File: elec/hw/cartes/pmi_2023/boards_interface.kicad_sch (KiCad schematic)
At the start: 39 parts, among them J10 Conn_01x01_Pin, J11 Conn_01x01_Socket, J12 Conn_01x01_Pin, J13 Conn_01x01_Pin, J14 Conn_01x01_Socket, J15 Conn_01x01_Socket, J16 Conn_01x01_Pin, J17 Conn_01x01_Pin, J18 Conn_01x01_Pin, J19 Conn_01x01_Pin, J20 Conn_01x01_Socket, J21 Conn_01x01_Socket, J22 Conn_01x01_Socket, J23 Conn_01x01_Pin, J24 Conn_01x01_Pin, J25 Conn_01x01_Pin, J26 Conn_01x01_Pin, J27 Conn_01x01_Socket, J28 Conn_01x01_Socket, J29 Conn_01x01_Socket, J30 Conn_01x01_Socket, J31 Conn_01x01_Pin, J32 Conn_01x01_Pin, J33 Conn_01x01_Socket, J34 Conn_01x01_Socket, J35 Conn_01x01_Pin, J36 Conn_01x01_Socket, J37 Conn_01x01_Pin, J38 Conn_01x01_Socket, J39 Conn_01x01_Pin, J40 Conn_01x01_Pin, J41 Conn_01x01_Socket, J42 Conn_01x01_Socket, J43 Conn_01x01_Socket, J44 Conn_01x01_Pin, J45 Conn_01x01_Socket, J46 Conn_01x01_Pin, J9 Conn_01x01_Socket

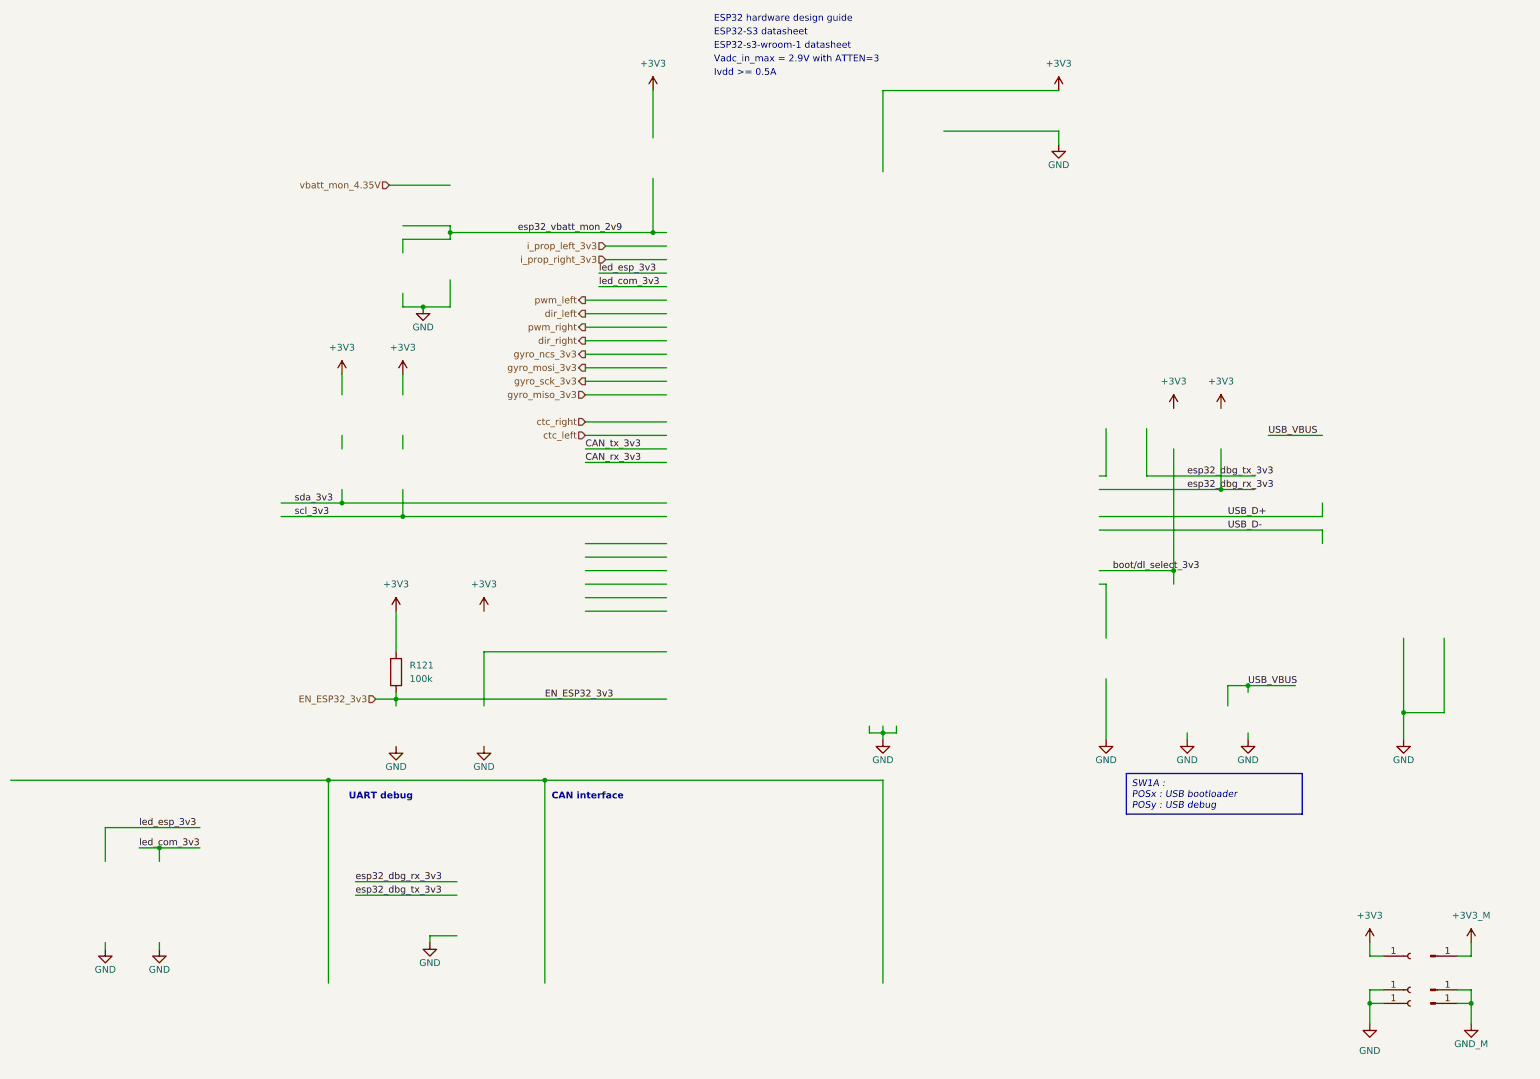
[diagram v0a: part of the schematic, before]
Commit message: pmi layout (WIP)
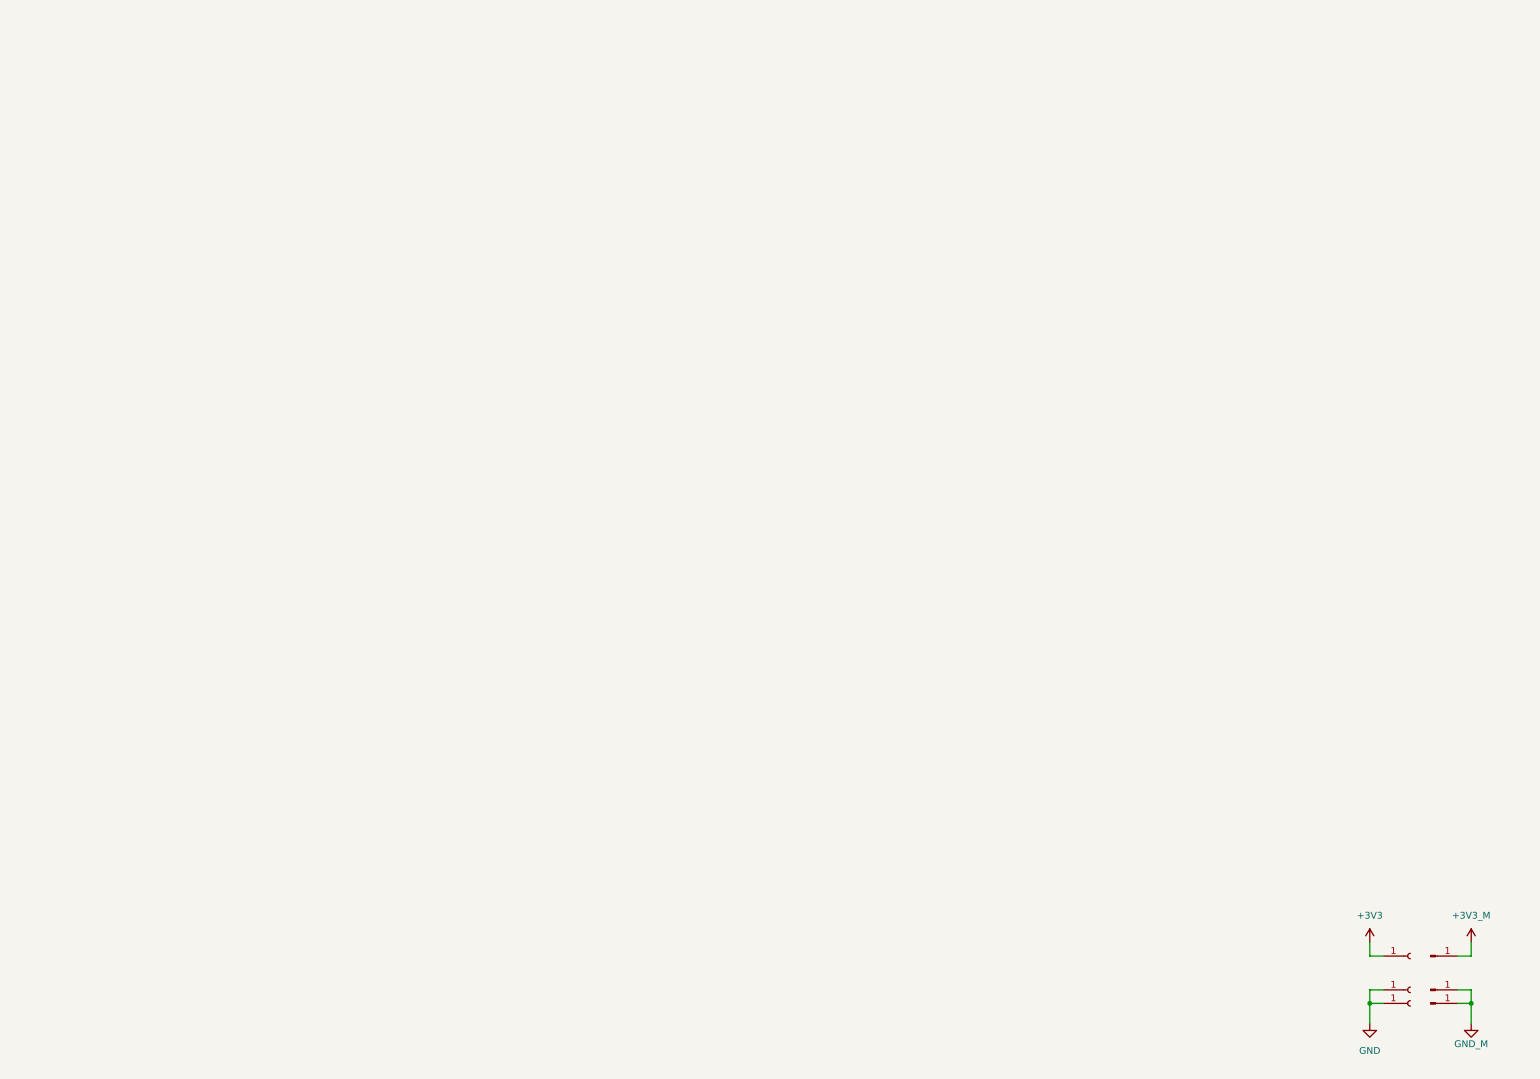
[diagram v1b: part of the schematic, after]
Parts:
- removed R121: 100k, cocotter_resistor:r0603_reflow, symbol cocotter_resistors:R_100k_0603_1%
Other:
- note removed: "CAN interface"
- note removed: "ESP32 hardware design guide"
- note removed: "ESP32-S3 datasheet"
- note removed: "ESP32-s3-wroom-1 datasheet"
- note removed: "Ivdd >= 0.5A"
- note removed: "UART debug"
- note removed: "Vadc_in_max = 2.9V with ATTEN=3"

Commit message: wip
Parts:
- added J47: Conn_01x01_Pin, cocotter_others:board_to_module_small, symbol Connector:Conn_01x01_Pin
- added J48: Conn_01x01_Socket, cocotter_others:board_to_module_small, symbol Connector:Conn_01x01_Socket
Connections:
- net com/vbatt_mon_4.35V: now also J47.1 (Pin_1)
- new net vbatt_mon_4.35V: J48.1 (Pin_1)
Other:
- sheet Sensor module ports: added gyro_irq_3v3; removed none
- sheet com ports: added emergency_stop_3v3, gyro_irq_3v3, start_robot_3v3; removed esp32_rx1_3v3, esp32_rx2_3v3, esp32_tx1_3v3, esp32_tx2_3v3
- sheet interface ports: added emergency_stop_3v3, start_robot_3v3; removed none

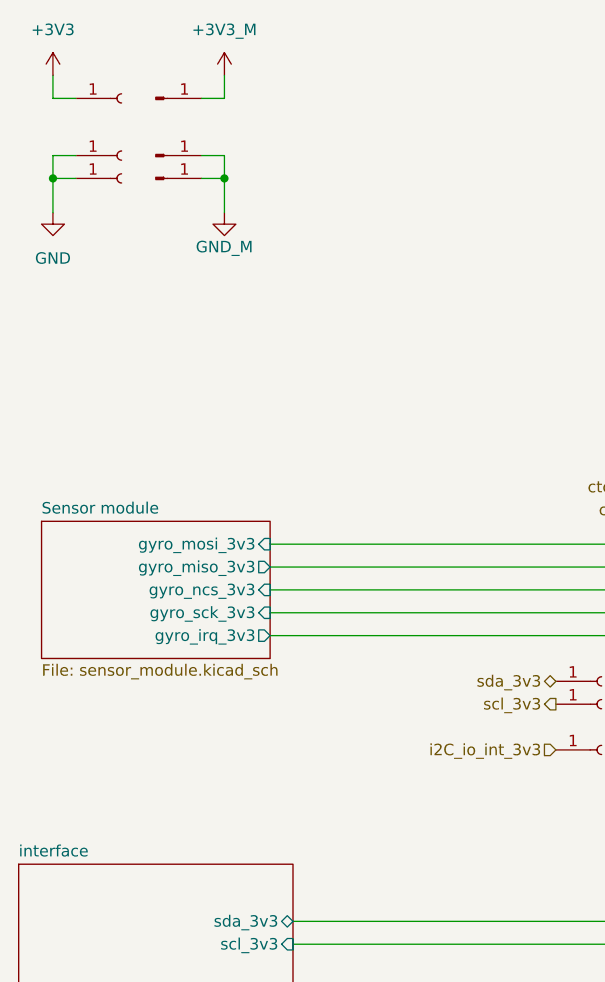
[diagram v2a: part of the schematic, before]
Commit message: front and back tof added, selector changed, ready to route
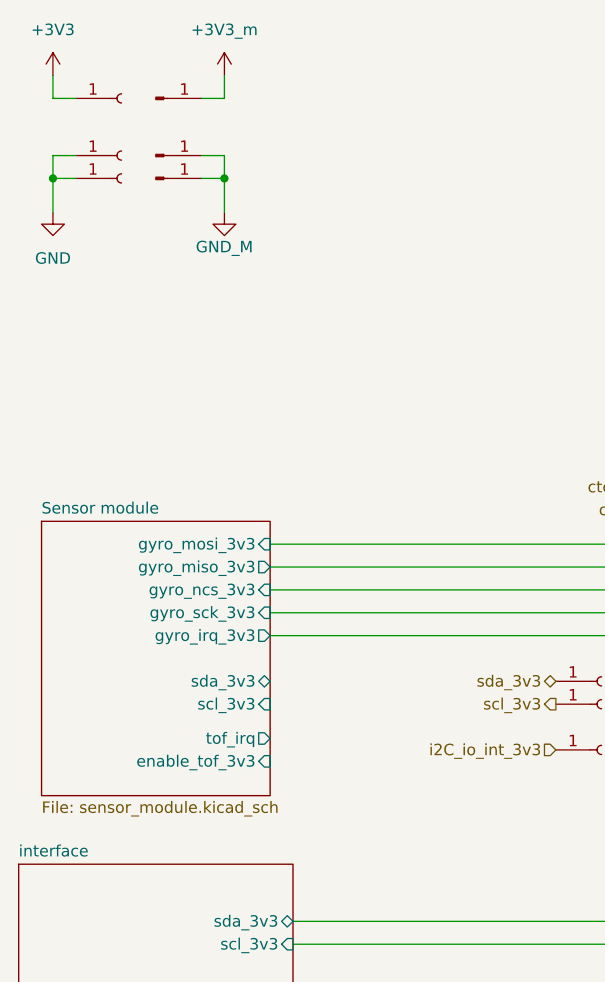
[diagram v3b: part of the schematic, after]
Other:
- sheet Sensor module ports: added enable_tof_3v3, scl_3v3, sda_3v3, tof_irq; removed none

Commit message: wip
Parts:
- removed J10, J12, J13, J16, J17, J18, J19, J23, J24, J25, J26, J31, J32, J35, J37, J39, J40, J44, J46, J47: Conn_01x01_Pin, cocotter_others:board_to_module_small, symbol Connector:Conn_01x01_Pin
- removed J11, J14, J15, J20, J21, J22, J27, J28, J29, J30, J33, J34, J36, J38, J41, J42, J43, J45, J48, J9: Conn_01x01_Socket, cocotter_others:board_to_module_small, symbol Connector:Conn_01x01_Socket
- added J49, J50: ~, pmi_2023_specific:pmi_2023_interconnection, symbol pmi_2023_specific:interconnect
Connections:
- net +3V3: now also J50.10 (P3V3)
- net +3V3_m: now also J49.10 (P3V3)
- net GND: now also J50.13 (GND), J50.7 (GND)
- net GND_M: now also J49.13 (GND), J49.7 (GND)
- net com/ctc_left: now also J49.20 (ctc_left_3v3)
- net com/ctc_right: now also J49.1 (ctc_right_3v3)
- net com/dir_left: now also J49.5 (DIR_left_3v3)
- net com/dir_right: now also J49.12 (dir_right_3v3)
- net com/i_prop_left_3v3: now also J49.6 (i_prop_left_3v3)
- net com/i_prop_right_3v3: now also J49.14 (i_prop_righ_3v3)
- net com/left_encod_A_3v3: now also J49.8 (left_encod_A_3v3)
- net com/left_encod_B_3v3: now also J49.9 (left_encod_B_3v3)
- net com/pwm_left: now also J49.4 (PWM_left_3v3)
- net com/pwm_right: now also J49.11 (pwm_right_3v3)
- net com/right_encod_A_3v3: now also J49.19 (right_encod_A_3v3)
- net com/right_encod_B_3v3: now also J49.18 (right_encod_B_3v3)
- net com/vbatt_mon_4.35V: now also J49.2 (vbat_mon_4.35V)
- net ctc_left: now also J50.20 (ctc_left_3v3)
- net ctc_right: now also J50.1 (ctc_right_3v3)
- net dir_left: now also J50.5 (DIR_left_3v3)
- net dir_right: now also J50.12 (dir_right_3v3)
- net i2C_io_int_3v3: now also J50.17 (i2c_to_int_3v3)
- net i_prop_left_3v3: now also J50.6 (i_prop_left_3v3)
- net i_prop_right_3v3: now also J50.14 (i_prop_righ_3v3)
- net left_encod_A_3v3: now also J50.8 (left_encod_A_3v3)
- net left_encod_B_3v3: now also J50.9 (left_encod_B_3v3)
- net pwm_left: now also J50.4 (PWM_left_3v3)
- net pwm_right: now also J50.11 (pwm_right_3v3)
- net right_encod_A_3v3: now also J50.19 (right_encod_A_3v3)
- net right_encod_B_3v3: now also J50.18 (right_encod_B_3v3)
- net scl_3v3: now also J50.15 (scl_3v3)
- net sda_3v3: now also J50.16 (sda_3v3)
- net tof_irq: now also J50.3 (tof_irq_3v3)
- net vbatt_mon_4.35V: now also J50.2 (vbat_mon_4.35V)
- new net i2c_io_int_3v3: J49.17 (i2c_to_int_3v3)
- new net scl_top_3v3: J49.15 (scl_3v3)
- new net sda_top_3v3: J49.16 (sda_3v3)
- new net tof_irq_3v3: J49.3 (tof_irq_3v3)
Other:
- sheet com ports: added conf3_3v3, enable_tof_3v3; removed none
- sheet interface ports: added conf3; removed none

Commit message: added oled display power supply res selectors, jlcpcb refs : wip
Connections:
- net +3V3_m is gone; now on net +3V3: J49.10 (P3V3)
- net GND_M is gone; now on net GND: J49.13 (GND), J49.7 (GND)
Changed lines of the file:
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@@
 			)
 		)
-		(property "Value" "GND_M"
+		(property "Value" "GND"
 			(at 186.69 118.11 0)
 			(effects
@@
 		(dnp no)
 		(property "Reference" "J49"
-			(at 209.55 61.214 0)
+			(at 210.058 52.324 0)
 			(effects
 				(font
@@
 		(dnp no)
 		(property "Reference" "J50"
-			(at 225.806 60.706 0)
+			(at 225.806 52.324 0)
 			(effects
 				(font
@@
 			)
 		)
-		(property "Value" "+3V3_m"
+		(property "Value" "+3V3"
 			(at 173.99 52.07 0)
 			(effects

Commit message: reset button added to esp32 reset. uart prog connector replaces ftdi one
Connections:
- net +3V3: no longer J49.10 (P3V3)
- net GND: no longer J49.13 (GND), J49.7 (GND)
- new net +3V3_m: J49.10 (P3V3)
- new net GND_m: J49.13 (GND), J49.7 (GND)
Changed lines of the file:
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@@
-	)
-	(symbol
-		(lib_id "power:GND")
-		(at 186.69 114.3 0)
-		(unit 1)
-		(exclude_from_sim no)
-		(in_bom yes)
-		(on_board yes)
-		(dnp no)
-		(property "Reference" "#PWR099"
-			(at 186.69 120.65 0)
-			(effects
-				(font
-					(size 1.27 1.27)
-				)
-				(hide yes)
-			)
-		)
-		(property "Value" "GND"
-			(at 186.69 118.11 0)
-			(effects
-				(font
-					(size 1.27 1.27)
-				)
-			)
-		)
-		(property "Footprint" ""
-			(at 186.69 114.3 0)
-			(effects
-				(font
-					(size 1.27 1.27)
-				)
-				(hide yes)
-			)
-		)
-		(property "Datasheet" ""
-			(at 186.69 114.3 0)
-			(effects
-				(font
-					(size 1.27 1.27)
-				)
-				(hide yes)
-			)
-		)
-		(property "Description" "Power symbol creates a global label with name \"GND\" , ground"
-			(at 186.69 114.3 0)
-			(effects
-				(font
-					(size 1.27 1.27)
-				)
-				(hide yes)
-			)
-		)
-		(pin "1"
-		)
-		(instances
-			(project "pmi_2023"
-				(path "/334a657f-c66c-4260-9567-14f1c99913d7/9da1923e-9bb0-4408-8ee2-582c85dcd497"
-					(reference "#PWR099")
-					(unit 1)
-				)
-			)
-		)
 	)
 	(symbol
@@
 	)
 	(symbol
+		(lib_id "pmi_2023_specific:GND_m")
+		(at 186.69 114.3 0)
+		(unit 1)
+		(exclude_from_sim no)
+		(in_bom yes)
+		(on_board yes)
+		(dnp no)
+		(fields_autoplaced yes)
+		(property "Reference" "#PWR091"
+			(at 186.69 120.65 0)
+			(effects
+				(font
+					(size 1.27 1.27)
+				)
+				(hide yes)
+			)
+		)
+		(property "Value" "GND_m"
+			(at 186.69 119.38 0)
+			(effects
+				(font
+					(size 1.27 1.27)
+				)
+			)
+		)
+		(property "Footprint" ""
+			(at 186.69 114.3 0)
+			(effects
+				(font
+					(size 1.27 1.27)
+				)
+				(hide yes)
+			)
+		)
+		(property "Datasheet" ""
+			(at 186.69 114.3 0)
+			(effects
+				(font
+					(size 1.27 1.27)
+				)
+				(hide yes)
+			)
+		)
+		(property "Description" "Power symbol creates a global label with name \"GND\" , ground"
+			(at 186.69 114.3 0)
+			(effects
+				(font
+					(size 1.27 1.27)
+				)
+				(hide yes)
+			)
+		)
+		(pin "1"
+		)
+		(instances
+			(project "pmi_2023"
+				(path "/334a657f-c66c-4260-9567-14f1c99913d7/9da1923e-9bb0-4408-8ee2-582c85dcd497"
+					(reference "#PWR091")
+					(unit 1)
+				)
+			)
+		)
+	)
+	(symbol
 		(lib_id "pmi_2023_specific:interconnect")
 		(at 198.12 85.09 0)
@@
 		(dnp no)
 		(property "Reference" "J49"
-			(at 210.058 52.324 0)
-			(effects
-				(font
-					(size 1.27 1.27)
-				)
-				(justify left)
+			(at 205.994 125.476 0)
+			(effects
+				(font
+					(size 1.27 1.27)
+				)
 			)
 		)
 		(property "Value" "~"
-			(at 214.63 85.09 0)
-			(effects
-				(font
-					(size 1.27 1.27)
-				)
-				(justify left)
+			(at 198.12 96.52 0)
+			(effects
+				(font
+					(size 1.27 1.27)
+				)
 			)
 		)
 		(property "Footprint" "pmi_2023_specific:pmi_2023_interconnection"
-			(at 198.12 96.52 0)
+			(at 198.12 93.98 0)
 			(effects
 				(font
@@
 		(dnp no)
 		(property "Reference" "J50"
-			(at 225.806 52.324 0)
-			(effects
-				(font
-					(size 1.27 1.27)
-				)
-				(justify left)
+			(at 229.616 125.476 0)
+			(effects
+				(font
+					(size 1.27 1.27)
+				)
 			)
 		)
 		(property "Value" "~"
-			(at 220.98 85.09 0)
-			(effects
-				(font
-					(size 1.27 1.27)
-				)
-				(justify left)
+			(at 237.49 96.52 0)
+			(effects
+				(font
+					(size 1.27 1.27)
+				)
 			)
 		)
 		(property "Footprint" "pmi_2023_specific:pmi_2023_interconnection"
-			(at 237.49 96.52 0)
+			(at 237.49 93.98 0)
 			(effects
 				(font
@@
 	)
 	(symbol
-		(lib_id "power:+3V3")
+		(lib_id "pmi_2023_specific:+3V3_m")
 		(at 173.99 57.15 0)
 		(unit 1)
@@
 		(dnp no)
 		(fields_autoplaced yes)
-		(property "Reference" "#PWR098"
+		(property "Reference" "#PWR097"
 			(at 173.99 60.96 0)
 			(effects
@@
 			)
 		)
-		(property "Value" "+3V3"
+		(property "Value" "+3V3_m"
 			(at 173.99 52.07 0)
 			(effects
@@
 			)
 		)
-		(property "Description" "Power symbol creates a global label with name \"+3V3\""
+		(property "Description" "Power symbol creates a global label with name \"+3V3_m\""
 			(at 173.99 57.15 0)
 			(effects
@@
 			(project "pmi_2023"
 				(path "/334a657f-c66c-4260-9567-14f1c99913d7/9da1923e-9bb0-4408-8ee2-582c85dcd497"
-					(reference "#PWR098")
-					(unit 1)
-				)
+					(reference "#PWR097")
+					(unit 1)
+				)

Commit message: pmi2023 : drc cleanup
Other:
- sheet Sensor module ports: added enable_back_tof_3v3, enable_front_tof_3v3; removed enable_tof_3v3
- sheet com ports: added enable_back_tof_3v3, enable_front_tof_3v3; removed enable_tof_3v3
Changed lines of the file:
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@@
+	(wire
+		(pts
+			(xy 57.15 100.33) (xy 113.03 100.33)
+		)
+		(stroke
+			(width 0)
+			(type default)
+		)
+	)
 	(wire
 		(pts
@@
 			)
 		)
-		(pin "enable_tof_3v3" input
+		(pin "enable_back_tof_3v3" output
+			(at 113.03 100.33 180)
+			(effects
+				(font
+					(size 1.27 1.27)
+				)
+				(justify left)
+			)
+		)
+		(pin "enable_front_tof_3v3" output
 			(at 113.03 97.79 180)
 			(effects
@@
 			)
 		)
-		(pin "enable_tof_3v3" input
+		(pin "enable_back_tof_3v3" input
+			(at 57.15 100.33 0)
+			(effects
+				(font
+					(size 1.27 1.27)
+				)
+				(justify right)
+			)
+		)
+		(pin "enable_front_tof_3v3" input
 			(at 57.15 97.79 0)
 			(effects
